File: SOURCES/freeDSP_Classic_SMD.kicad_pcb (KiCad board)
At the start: 2 copper layers, 170 parts, among them J1 RCA_01, J2 RCA_01, J3 CONN_01X02, J4 RCA_01, J5 RCA_01, J6 RCA_01, J7 RCA_01, P1 CONN_01X06, P2 CONN_01X03, P3 CONN_02X05, P4 STDCONN, P5 STDCONN, P6 STDCONN, P7 STDCONN, P8 CONN_02X03, P9 CONN_02X03, Q1 BSS123, Q10 BSH103,215, Q11 BSH103,215, Q12 BSH103,215, Q13 BSH103,215, Q14 MMBF5434, Q15 MMBF5434, Q16 MMBF5434, Q17 MMBF5434, Q18 BSS123, Q2 BSS123, Q3 BSS123, Q4 BSS123, Q5 FZT751TA, Q6 BSH103,215, Q7 BSH103,215, Q8 BSH103,215, Q9 BSH103,215, SW1 SW_PUSH, U1 ADAU1701, U2 24AA256SN, U3 LME49721, U4 LME49721, U5 SN74LVC3G14, U6 LM393, U7 IDT2305NZ, X1 ASV-24.576MHz-EJ-T

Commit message: improved layout
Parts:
- moved C8 17.5 mm to (118.6, 151.4)
- moved FB2 8.26 mm to (85.3, 132.1), turned to 90 degrees
- moved C10 5.62 mm to (102.4, 150.4), turned to 270 degrees
- moved R7 2.54 mm to (80.5, 131.1)
- moved P2 0.85 mm to (77.2, 134.6)
- moved C54 0.32 mm to (89.7, 127.3)
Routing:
- net +3V3: track 376.2 -> 398.5 mm, vias 6 -> 7
- net BRD_RST: track 207.6 -> 228.5 mm
- net Net-(C54-Pad1): track 25.3 -> 34.3 mm, vias 0 -> 2
- net GND: track 1022.5 -> 1016.5 mm
- net Net-(P2-Pad2): track 15.4 -> 18.0 mm, vias 0 -> 1
- net WP: track 114.0 -> 115.4 mm
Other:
- net class ADAU: via_dia 0.6 -> 0.7; via_drill 0.4 -> 0.3
- net class Default: via_dia 0.6 -> 0.7; via_drill 0.4 -> 0.3
- net class Supply: via_dia 0.6 -> 0.7; via_drill 0.4 -> 0.3
- rule via_min_size: 0.4 -> 0.3

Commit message: layout improvements
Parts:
- C54: value 10n -> 10u
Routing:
- net +3V3: track 398.5 -> 422.4 mm
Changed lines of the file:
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@@
     (links 410)
     (no_connects 0)
-    (area 54.327429 56.339 152.682572 159.661)
+    (area 0 0 0 0)
     (thickness 1.6)
     (drawings 10)
-    (tracks 2222)
+    (tracks 2225)
     (zones 0)
     (modules 170)
@@
       (effects (font (size 1 1) (thickness 0.15)))
     )
-    (fp_text value 10n (at 0 2.3 180) (layer F.Fab)
+    (fp_text value 10u (at 0 2.3 180) (layer F.Fab)
       (effects (font (size 1 1) (thickness 0.15)))
     )
@@
   (segment (start 111.5695 117.2845) (end 108.2675 117.2845) (width 0.25) (layer F.Cu) (net 3))
   (segment (start 112.4445 118.3255) (end 112.4445 118.201502) (width 0.25) (layer F.Cu) (net 3))
+  (segment (start 102.362 152.368) (end 102.362 153.797) (width 0.6) (layer F.Cu) (net 4))
+  (segment (start 82.042 155.956) (end 79.1845 153.0985) (width 0.6) (layer F.Cu) (net 4))
+  (segment (start 100.203 155.956) (end 82.042 155.956) (width 0.6) (layer F.Cu) (net 4))
+  (segment (start 102.362 153.797) (end 100.203 155.956) (width 0.6) (layer F.Cu) (net 4))
   (segment (start 82.518 131.064) (end 83.078 131.064) (width 0.6) (layer F.Cu) (net 4))
   (segment (start 83.078 131.064) (end 85.344 133.33) (width 0.6) (layer F.Cu) (net 4))
@@
   (segment (start 115.062 151.13) (end 115.062 148.59) (width 0.6) (layer F.Cu) (net 4))
   (segment (start 113.824 152.368) (end 113.792 152.4) (width 0.6) (layer F.Cu) (net 4))
-  (segment (start 102.362 152.368) (end 99.568 152.368) (width 0.6) (layer F.Cu) (net 4))
   (segment (start 99.568 152.368) (end 99.568 152.4) (width 0.6) (layer F.Cu) (net 4))
   (segment (start 76.327 136.779) (end 76.327 137.541) (width 0.6) (layer F.Cu) (net 4))
-  (via (at 76.454 137.668) (size 0.7) (drill 0.3) (layers F.Cu B.Cu) (net 4))
+  (segment (start 76.454 137.668) (end 76.454 150.368) (width 0.6) (layer B.Cu) (net 4))
+  (segment (start 79.1845 153.0985) (end 76.454 150.368) (width 0.6) (layer B.Cu) (net 4))
   (segment (start 76.327 137.541) (end 76.454 137.668) (width 0.6) (layer F.Cu) (net 4))
+  (via (at 76.454 137.668) (size 0.7) (drill 0.3) (layers F.Cu B.Cu) (net 4))
   (segment (start 87.8205 133.33) (end 87.8205 133.35) (width 0.6) (layer F.Cu) (net 4))
   (segment (start 102.87 141.986) (end 102.87 144.812) (width 0.6) (layer F.Cu) (net 4))
@@
   (segment (start 118.618 148.844) (end 118.364 148.59) (width 0.6) (layer F.Cu) (net 4))
   (segment (start 118.364 148.59) (end 118.618 149.384) (width 0.6) (layer F.Cu) (net 4))
-  (segment (start 79.1845 153.0985) (end 76.454 150.368) (width 0.6) (layer B.Cu) (net 4))
-  (segment (start 76.454 137.668) (end 76.454 150.368) (width 0.6) (layer B.Cu) (net 4))
   (segment (start 101.06 134.068) (end 101.06 134.334) (width 0.2) (layer F.Cu) (net 4))
   (segment (start 99.568 136.144) (end 99.568 136.017) (width 0.2) (layer F.Cu) (net 4))
@@
   (segment (start 82.296 153.8285) (end 83.6295 153.8285) (width 0.6) (layer F.Cu) (net 4))
   (segment (start 79.1845 153.0985) (end 79.9145 153.8285) (width 0.6) (layer F.Cu) (net 4))
+  (segment (start 82.296 153.8285) (end 79.9145 153.8285) (width 0.6) (layer F.Cu) (net 4))
   (segment (start 126.335 93.296) (end 126.335 92.394) (width 0.3) (layer F.Cu) (net 4))
   (segment (start 126.335 92.394) (end 124.492 90.551) (width 0.3) (layer F.Cu) (net 4))
@@
   (segment (start 86.8545 153.7785) (end 86.8045 153.8285) (width 0.6) (layer F.Cu) (net 4))
   (segment (start 86.8045 153.8285) (end 82.296 153.8285) (width 0.6) (layer F.Cu) (net 4))
-  (segment (start 82.296 153.8285) (end 79.9145 153.8285) (width 0.6) (layer F.Cu) (net 4))
   (segment (start 86.8545 153.7785) (end 86.8045 153.8285) (width 0.3) (layer F.Cu) (net 4))
   (segment (start 112.268 139.986) (end 112.268 136.906) (width 0.25) (layer F.Cu) (net 5))

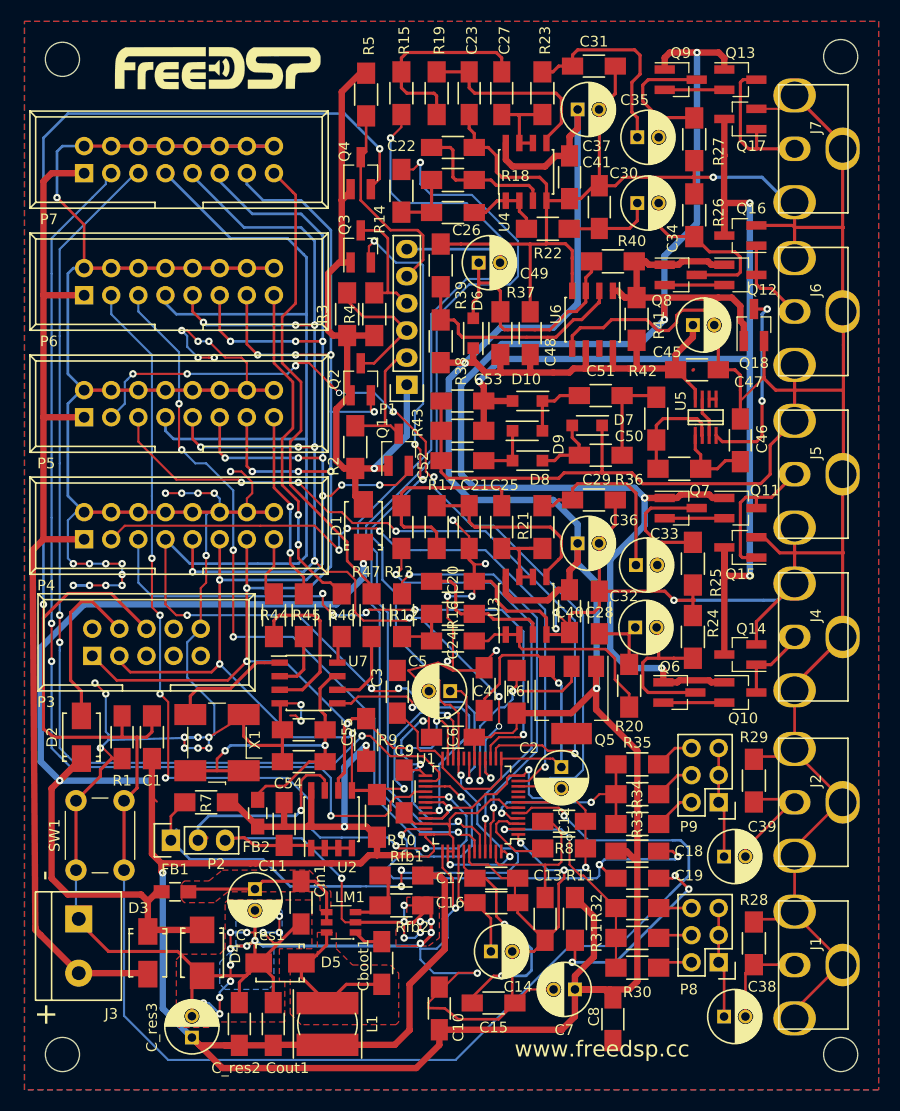
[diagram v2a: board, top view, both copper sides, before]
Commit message: added fiducials
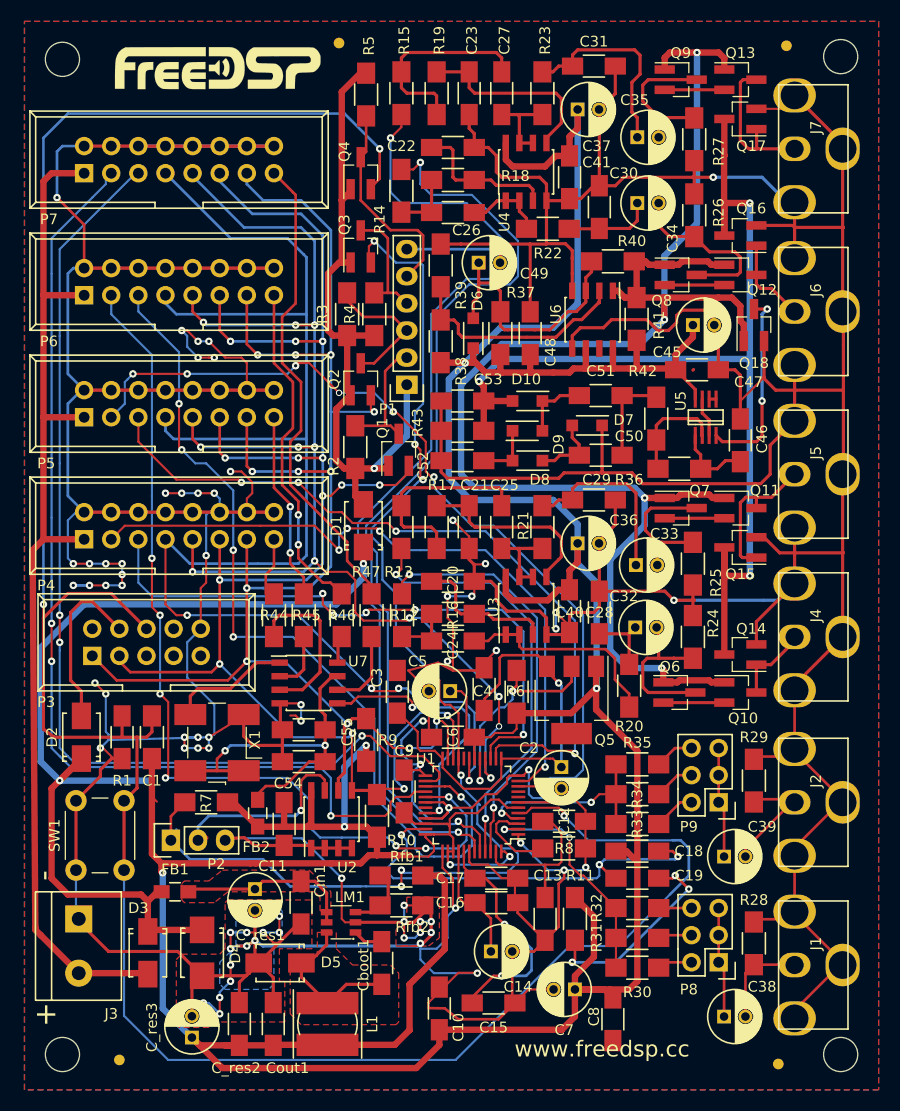
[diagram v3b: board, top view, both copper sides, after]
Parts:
- added REF**: FIDUCIAL_1MM_DOT, fdsp_fiducial:FIDUCIAL_1MM_DOT, F.Cu at (93.0, 59.9)
- added REF**: FIDUCIAL_1MM_DOT, fdsp_fiducial:FIDUCIAL_1MM_DOT, F.Cu at (134.1, 155.6)
- added REF**: FIDUCIAL_1MM_DOT, fdsp_fiducial:FIDUCIAL_1MM_DOT, F.Cu at (72.4, 155.2)
- added REF**: FIDUCIAL_1MM_DOT, fdsp_fiducial:FIDUCIAL_1MM_DOT, F.Cu at (134.9, 60.2)
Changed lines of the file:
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@@
     (links 410)
     (no_connects 0)
-    (area 0 0 0 0)
+    (area 54.327429 56.339 152.682572 159.661)
     (thickness 1.6)
     (drawings 10)
     (tracks 2225)
     (zones 0)
-    (modules 170)
+    (modules 174)
     (nets 116)
   )
@@
       (xy 0.228721 -0.6985) (xy 0.235911 -0.668229)) (layer F.SilkS) (width 0.01))
   )
+  (module fdsp_fiducial:FIDUCIAL_1MM_DOT (layer F.Cu)
+    (at 92.964 59.944)
+    (fp_text reference REF** (at 0.1 2.9) (layer F.Fab)
+      (effects (font (size 1 1) (thickness 0.15)))
+    )
+    (fp_text value FIDUCIAL_1MM_DOT (at 0 -3) (layer F.Fab)
+      (effects (font (size 1 1) (thickness 0.15)))
+    )
+    (pad 1 smd circle (at 0 0) (size 1 1) (layers *.Cu *.SilkS *.Mask)
+      (solder_mask_margin 1.5) (solder_paste_margin 1.5) (clearance 1.5) (zone_connect 0))
+  )
+  (module fdsp_fiducial:FIDUCIAL_1MM_DOT (layer F.Cu)
+    (at 134.112 155.575)
+    (fp_text reference REF** (at 0.1 2.9) (layer F.Fab)
+      (effects (font (size 1 1) (thickness 0.15)))
+    )
+    (fp_text value FIDUCIAL_1MM_DOT (at 0 -3) (layer F.Fab)
+      (effects (font (size 1 1) (thickness 0.15)))
+    )
+    (pad 1 smd circle (at 0 0) (size 1 1) (layers *.Cu *.SilkS *.Mask)
+      (solder_mask_margin 1.5) (solder_paste_margin 1.5) (clearance 1.5) (zone_connect 0))
+  )
+  (module fdsp_fiducial:FIDUCIAL_1MM_DOT (layer F.Cu)
+    (at 72.39 155.194)
+    (fp_text reference REF** (at 0.1 2.9) (layer F.Fab)
+      (effects (font (size 1 1) (thickness 0.15)))
+    )
+    (fp_text value FIDUCIAL_1MM_DOT (at 0 -3) (layer F.Fab)
+      (effects (font (size 1 1) (thickness 0.15)))
+    )
+    (pad 1 smd circle (at 0 0) (size 1 1) (layers *.Cu *.SilkS *.Mask)
+      (solder_mask_margin 1.5) (solder_paste_margin 1.5) (clearance 1.5) (zone_connect 0))
+  )
+  (module fdsp_fiducial:FIDUCIAL_1MM_DOT (layer F.Cu)
+    (at 134.874 60.198)
+    (fp_text reference REF** (at 0.1 2.9) (layer F.Fab)
+      (effects (font (size 1 1) (thickness 0.15)))
+    )
+    (fp_text value FIDUCIAL_1MM_DOT (at 0 -3) (layer F.Fab)
+      (effects (font (size 1 1) (thickness 0.15)))
+    )
+    (pad 1 smd circle (at 0 0) (size 1 1) (layers *.Cu *.SilkS *.Mask)
+      (solder_mask_margin 1.5) (solder_paste_margin 1.5) (clearance 1.5) (zone_connect 0))
+  )
   (gr_text "Max Becker\nKai Dehmelt\nChristoph Schmidt\nMax Wulf" (at 104.648 76.708 270) (layer B.SilkS)

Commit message: some improvements
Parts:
- removed the REF** at (93.0, 59.9)
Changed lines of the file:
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@@
     (links 410)
     (no_connects 0)
-    (area 54.327429 56.339 152.682572 159.661)
+    (area 54.327429 55.869 152.682572 159.661)
     (thickness 1.6)
     (drawings 10)
     (tracks 2225)
     (zones 0)
-    (modules 174)
+    (modules 173)
     (nets 116)
   )
@@
   (layers
     (0 F.Cu signal)
-    (31 B.Cu signal)
+    (31 B.Cu signal hide)
     (32 B.Adhes user)
     (33 F.Adhes user)
@@
   )
   (module fdsp_fiducial:FIDUCIAL_1MM_DOT (layer F.Cu)
-    (at 92.964 59.944)
-    (fp_text reference REF** (at 0.1 2.9) (layer F.Fab)
-      (effects (font (size 1 1) (thickness 0.15)))
-    )
-    (fp_text value FIDUCIAL_1MM_DOT (at 0 -3) (layer F.Fab)
-      (effects (font (size 1 1) (thickness 0.15)))
-    )
-    (pad 1 smd circle (at 0 0) (size 1 1) (layers *.Cu *.SilkS *.Mask)
-      (solder_mask_margin 1.5) (solder_paste_margin 1.5) (clearance 1.5) (zone_connect 0))
-  )
-  (module fdsp_fiducial:FIDUCIAL_1MM_DOT (layer F.Cu)
